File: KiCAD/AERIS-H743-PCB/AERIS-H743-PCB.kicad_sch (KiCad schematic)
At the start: 0 parts

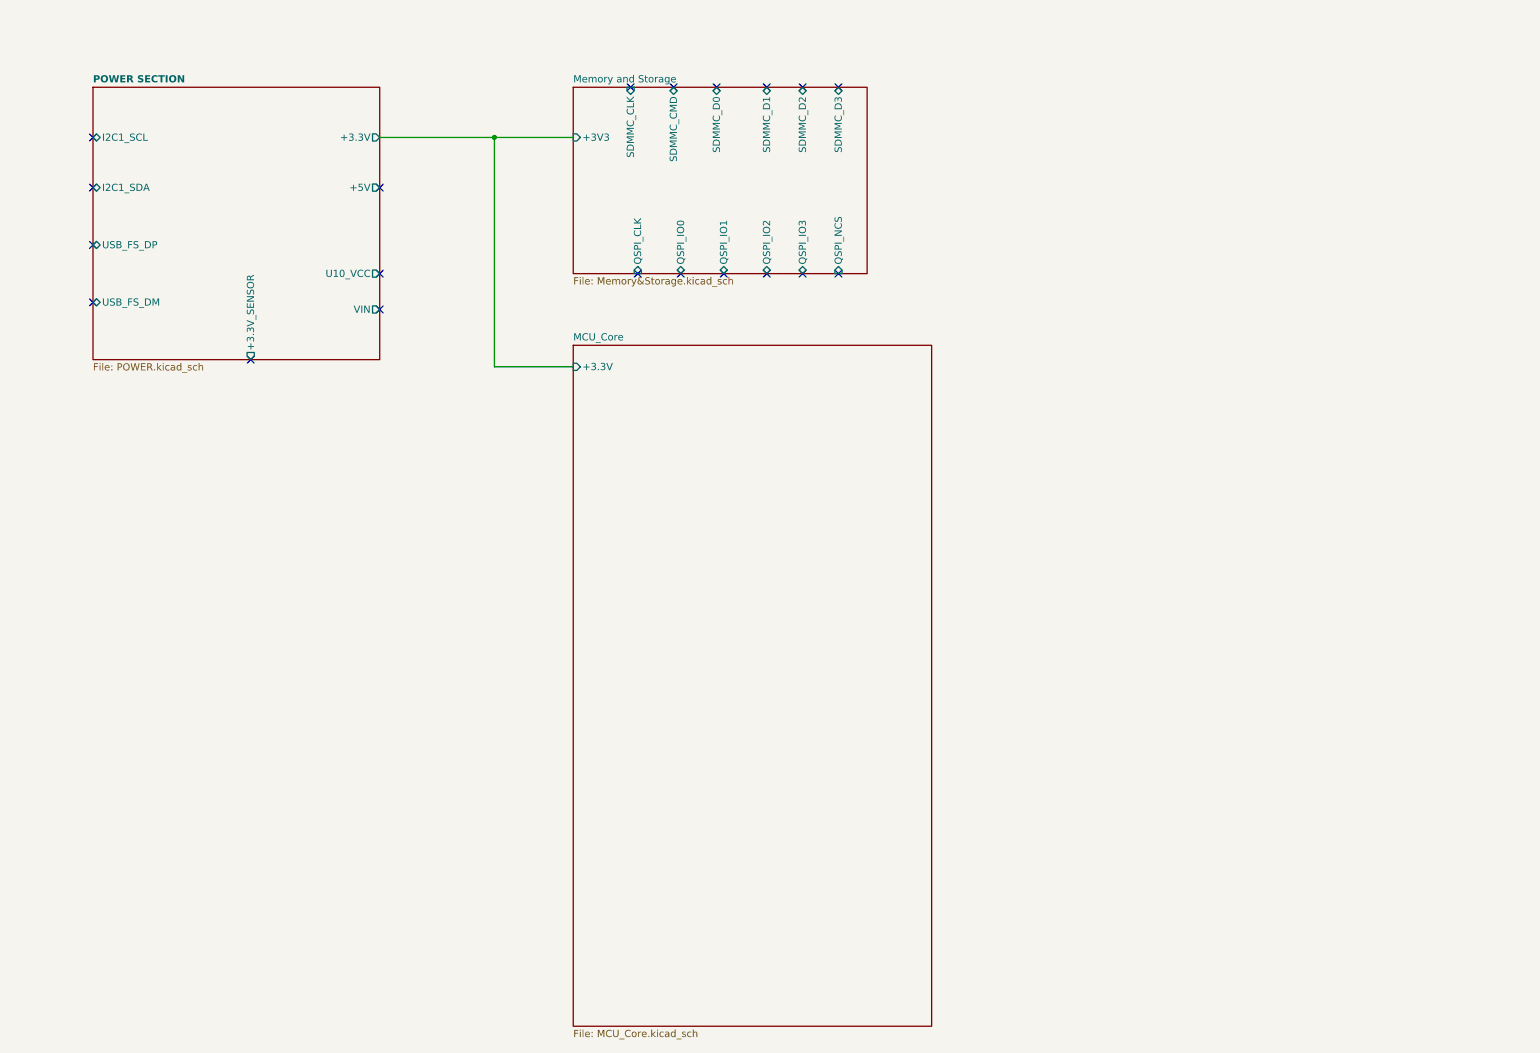
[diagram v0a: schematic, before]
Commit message: Sensor Sheet Updated
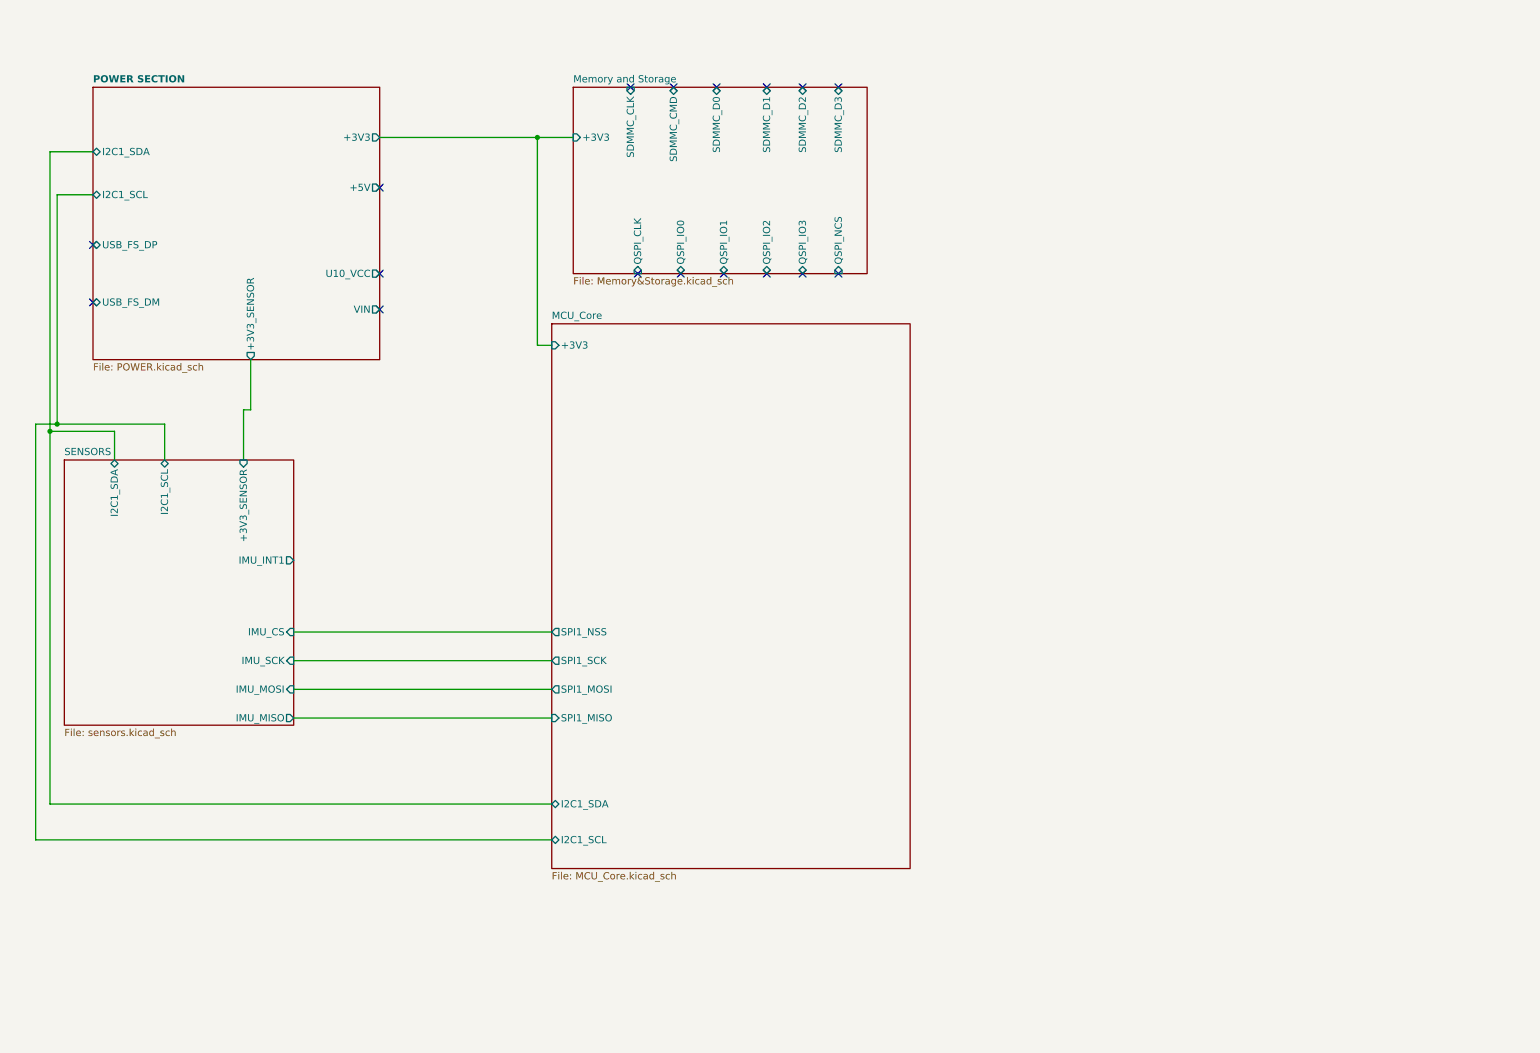
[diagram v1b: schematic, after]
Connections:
- no-connect marks 20 -> 17
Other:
- added sheet SENSORS (sensors.kicad_sch)
- sheet MCU_Core ports: added +3V3, I2C1_SCL, I2C1_SDA, SPI1_MISO, SPI1_MOSI, SPI1_NSS, SPI1_SCK; removed +3.3V
- sheet POWER SECTION ports: added +3V3, +3V3_SENSOR; removed +3.3V, +3.3V_SENSOR

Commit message: update
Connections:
- no-connect marks 17 -> 18
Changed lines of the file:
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@@
+	)
+	(no_connect
+		(at 60.96 109.22)
 	)
 	(no_connect

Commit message: all sheet available
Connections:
- no-connect marks 18 -> 29
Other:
- added sheet COMMUNICATION (Communication.kicad_sch)
- added sheet Connectors and Indicators (Conn&Inc.kicad_sch)

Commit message: Updated and complete Schematic
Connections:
- no-connect marks 29 -> 1
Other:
- sheet COMMUNICATION ports: added none; removed A, B, CANH, CANL
- sheet Connectors and Indicators ports: added +3V3, PE11, PE13, PE14, PE9, RGB_B, RGB_G, RGB_R, Status_LED, USER_BTN; removed none
- sheet MCU_Core ports: added ESC1_PWM, ESC2_PWM, ESC3_PWM, ESC4_PWM, FDCAN_RX, FDCAN_TX, GPS_RX, GPS_TX, IMU_INT1, QSPI_CLK, QSPI_IO0, QSPI_IO1, QSPI_IO2, QSPI_IO3, QSPI_NCS, RGB_B, RGB_G, RGB_R, RS485_DE, RS485_RX, RS485_TX, SDMMC_CLK, SDMMC_CMD, SDMMC_D0, SDMMC_D1, SDMMC_D2, SDMMC_D3, Status_LED, USB_DP, USER_BTN, USP_DM; removed none
- sheet POWER SECTION ports: added none; removed U10_VCC, VIN

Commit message: update
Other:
- sheet POWER SECTION ports: added USB_DM, USB_DP; removed USB_FS_DM, USB_FS_DP
- sheet SENSORS ports: added SPI1_MISO, SPI1_MOSI, SPI1_NSS, SPI1_SCK; removed IMU_CS, IMU_MISO, IMU_MOSI, IMU_SCK
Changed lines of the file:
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@@
 			)
 		)
-		(pin "USB_FS_DM" bidirectional
+		(pin "USB_DM" bidirectional
 			(at 25.4 63.5 180)
 			(effects
@@
 			)
 		)
-		(pin "USB_FS_DP" bidirectional
+		(pin "USB_DP" bidirectional
 			(at 25.4 53.34 180)
 			(effects
@@
 			)
 		)
-		(pin "IMU_CS" input
+		(pin "SPI1_NSS" input
 			(at 60.96 121.92 0)
 			(effects
@@
 			)
 		)
-		(pin "IMU_MISO" output
+		(pin "SPI1_MISO" output
 			(at 60.96 137.16 0)
 			(effects
@@
 			)
 		)
-		(pin "IMU_MOSI" input
+		(pin "SPI1_MOSI" input
 			(at 60.96 132.08 0)
 			(effects
@@
 			)
 		)
-		(pin "IMU_SCK" input
+		(pin "SPI1_SCK" input
 			(at 60.96 127 0)
 			(effects
